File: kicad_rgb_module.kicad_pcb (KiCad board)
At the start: 2 copper layers, 25 x 25 mm, 37 parts, among them J1 Conn_HackConnect, SW1 TS-1088-AR02016, U1 STM32G030F6P6, U2 NCP114ASN330T1G

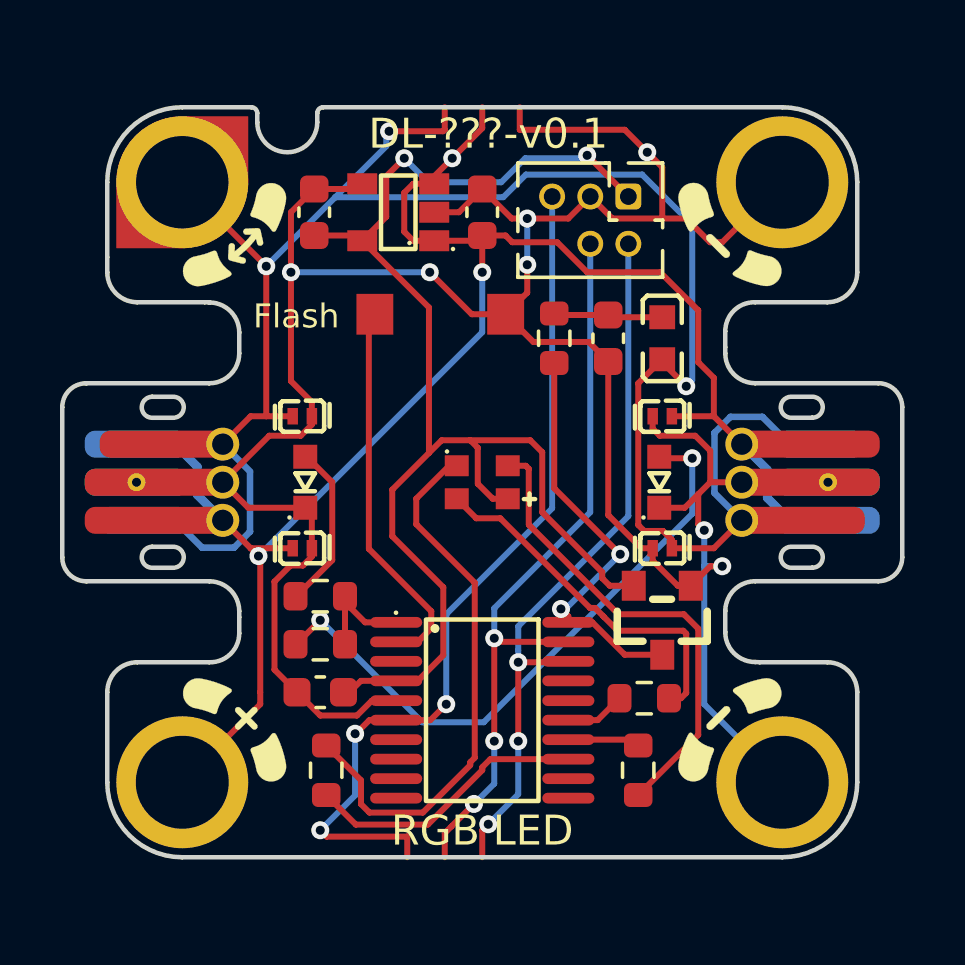
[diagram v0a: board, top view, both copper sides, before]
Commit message: Add diode to nRESET, decide on board sides for GerberSockets
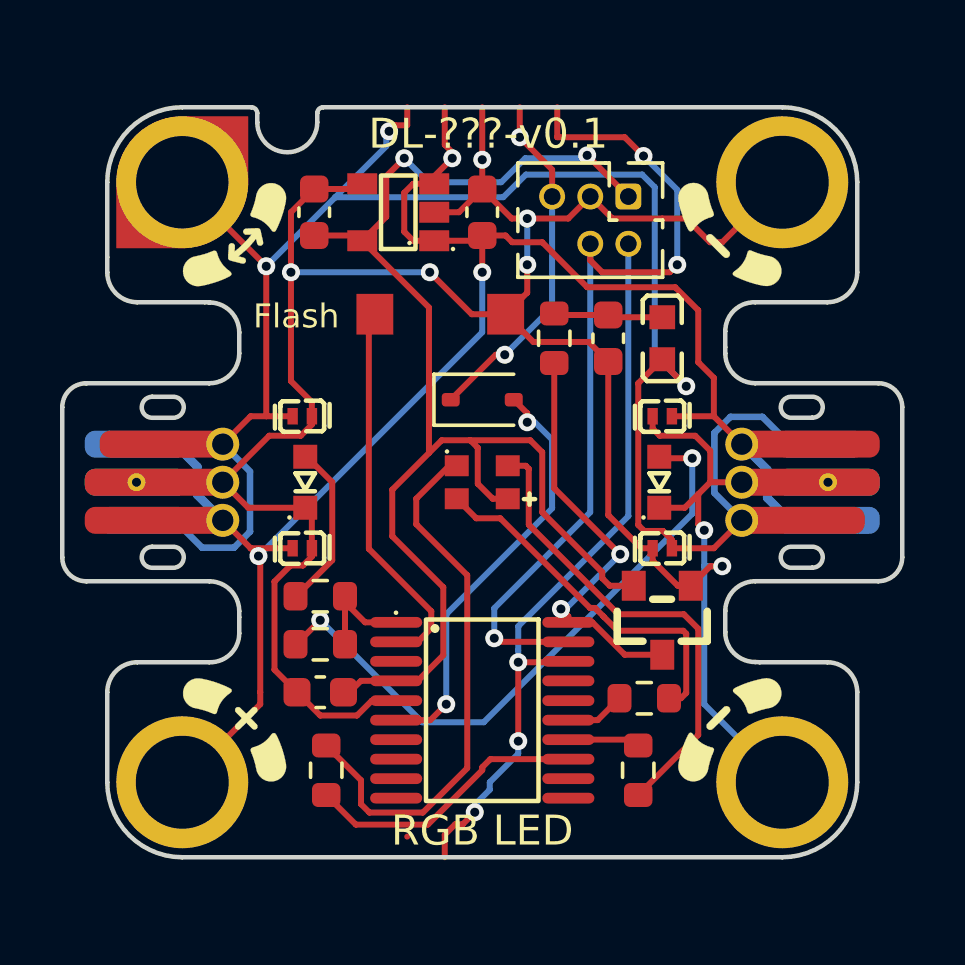
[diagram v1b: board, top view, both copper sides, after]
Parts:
- added D9: 1N4148WS, Diode_SMD:D_SOD-323, F.Cu at (85.5, 72.2)
- moved GS4 25.3 mm to (86.8, 62.5), turned to 180 degrees
- moved GS5 25.3 mm to (88.0, 62.5), turned to 180 degrees
- moved GS1 1.25 mm to (85.5, 62.5)
- moved GS2 1.25 mm to (83.0, 62.5)
- moved GS3 1.25 mm to (84.2, 62.5)
- moved GS6 1.25 mm to (84.2, 87.5)
- moved GS7 1.25 mm to (85.5, 87.5)
- moved GS8 1.25 mm to (86.8, 87.5)
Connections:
- GS4 pad 1: /nRESET -> /nRESET-SAFE
- J1 pad 5: /nRESET -> /nRESET-SAFE
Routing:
- net /nRESET: track 29.2 -> 14.2 mm, vias 3 -> 2
- net /nRESET-SAFE: track 0.00 -> 11.8 mm, vias 0 -> 2
- net GND: track 95.3 -> 90.3 mm
- net /SWCLK: track 25.2 -> 28.9 mm
- net /JD_DATA: track 50.3 -> 48.8 mm
- net /SWDIO: track 24.1 -> 24.8 mm

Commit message: Swap sides of GerberSockets, add devices-lab logo and hwidx QR code
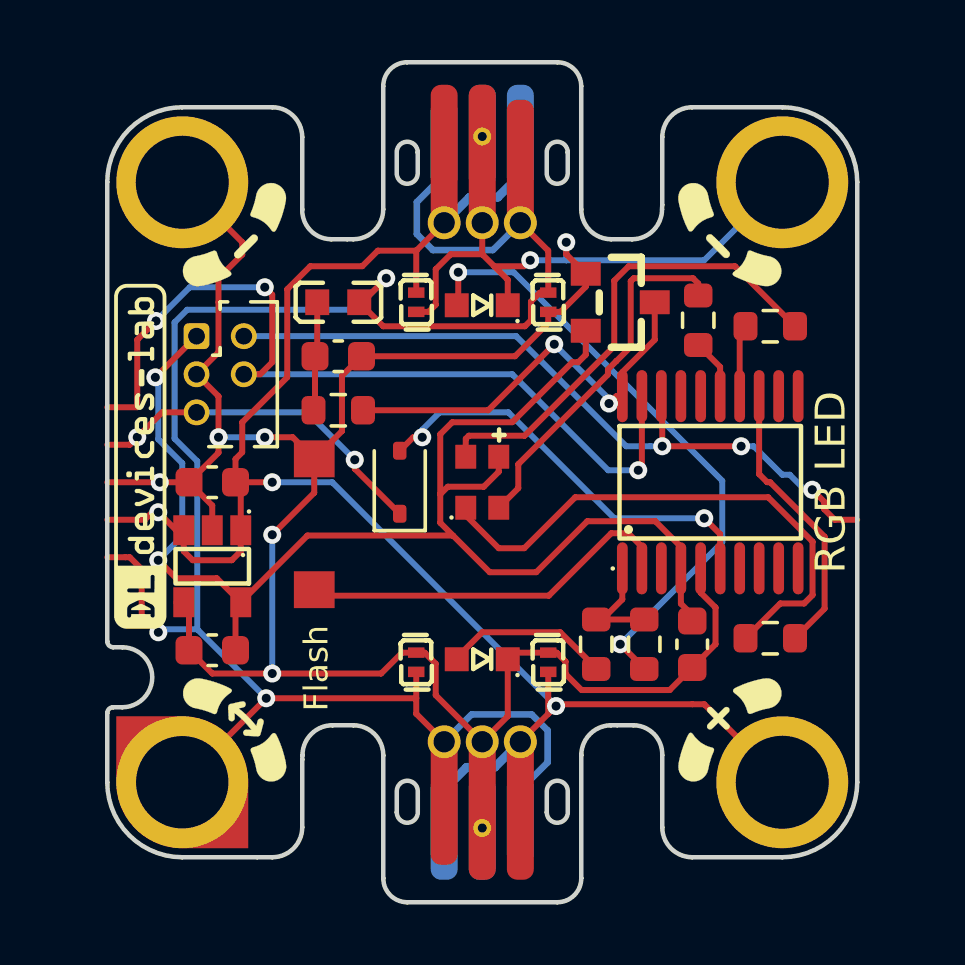
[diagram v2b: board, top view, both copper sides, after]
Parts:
- added G***: LOGO, LOGO, F.Cu at (74.1, 74.1)
- added G***: LOGO, LOGO, B.Cu at (85.5, 75.0)
- moved MH1 20.0 mm to (75.5, 85.0), turned to 90 degrees
- moved MH2 20.0 mm to (75.5, 65.0), turned to 90 degrees
- moved MH3 20.0 mm to (95.5, 85.0), turned to 90 degrees
- moved MH4 20.0 mm to (95.5, 65.0), turned to 90 degrees
- moved GS2 18.0 mm to (73.0, 77.5), turned to 90 degrees
- moved GS5 18.0 mm to (73.0, 72.5), turned to -90 degrees
- moved GS3 17.8 mm to (73.0, 76.2), turned to 90 degrees
- moved GS4 17.8 mm to (73.0, 73.8), turned to -90 degrees
- moved GS6 17.8 mm to (98.0, 76.2), turned to 90 degrees
- moved GS8 17.8 mm to (98.0, 73.8), turned to 90 degrees
- moved GS1 17.7 mm to (73.0, 75.0), turned to 90 degrees
- moved GS7 17.7 mm to (98.0, 75.0), turned to 90 degrees
- moved R4 15.4 mm to (95.1, 80.2), turned to 0 degrees
- moved R5 15.4 mm to (95.1, 69.8), turned to 180 degrees
- moved C4 15.0 mm to (76.5, 80.6), turned to 180 degrees
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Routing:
- net /JD_DATA: track 48.8 -> 49.5 mm
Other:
- outline, holes or cut-outs redrawn

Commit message: Set the correct LCSC components
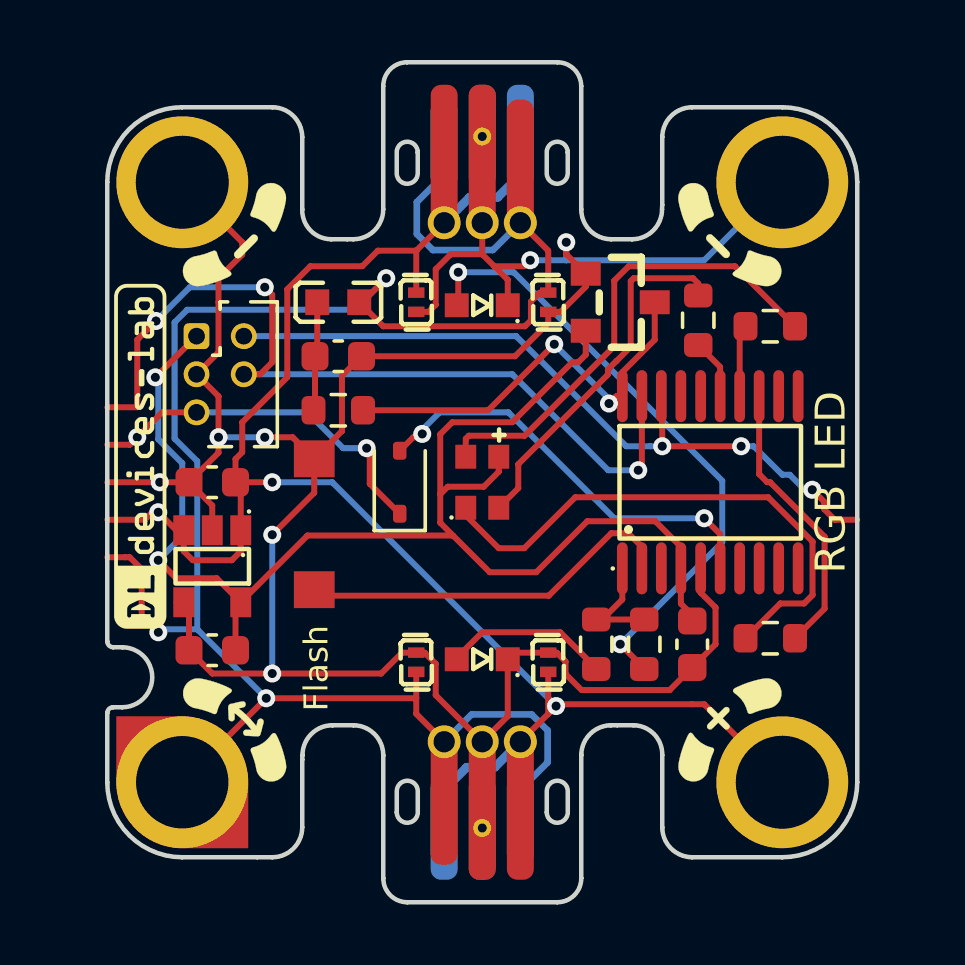
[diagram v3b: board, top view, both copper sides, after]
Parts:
- D8: value NH-B2020RGBA-HF -> NH-B2020RGBA-GF
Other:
- board text removed: "DL-???-v0.1"

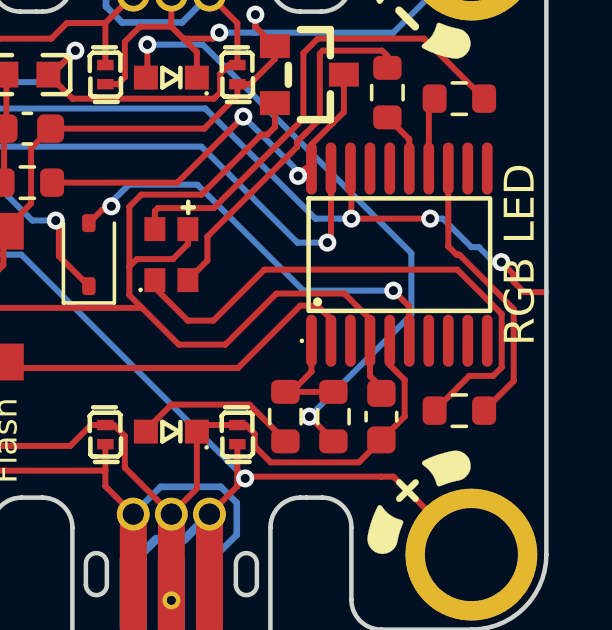
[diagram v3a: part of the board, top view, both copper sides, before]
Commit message: Change some GerberSockets and components
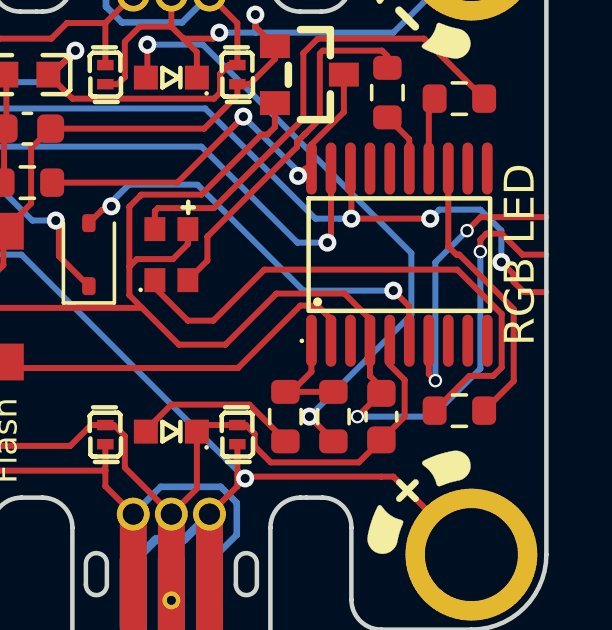
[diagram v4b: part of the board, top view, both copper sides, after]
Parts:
- GS7: value TEST_1 -> 3V3; footprint GerberSockets:TEST_1 -> GerberSockets:3V3
- GS8: value TEST_2 -> SERIAL; footprint GerberSockets:TEST_2 -> GerberSockets:SERIAL
- MH1: value jacdac_hole_DATA_MH1 -> Val**
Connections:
- GS7 pad 1: unconnected-(GS7-TEST_1-Pad1) -> +3V3
- GS8 pad 1: unconnected-(GS8-TEST_2-Pad1) -> /SERIAL
- U1 pad 7: unconnected-(U1-PA0-Pad7) -> /SERIAL
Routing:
- net +3V3: track 46.5 -> 59.3 mm, vias 2 -> 4
- net /SERIAL: track 0.00 -> 9.69 mm, vias 0 -> 2
- net /SWDIO: track 24.8 -> 25.7 mm

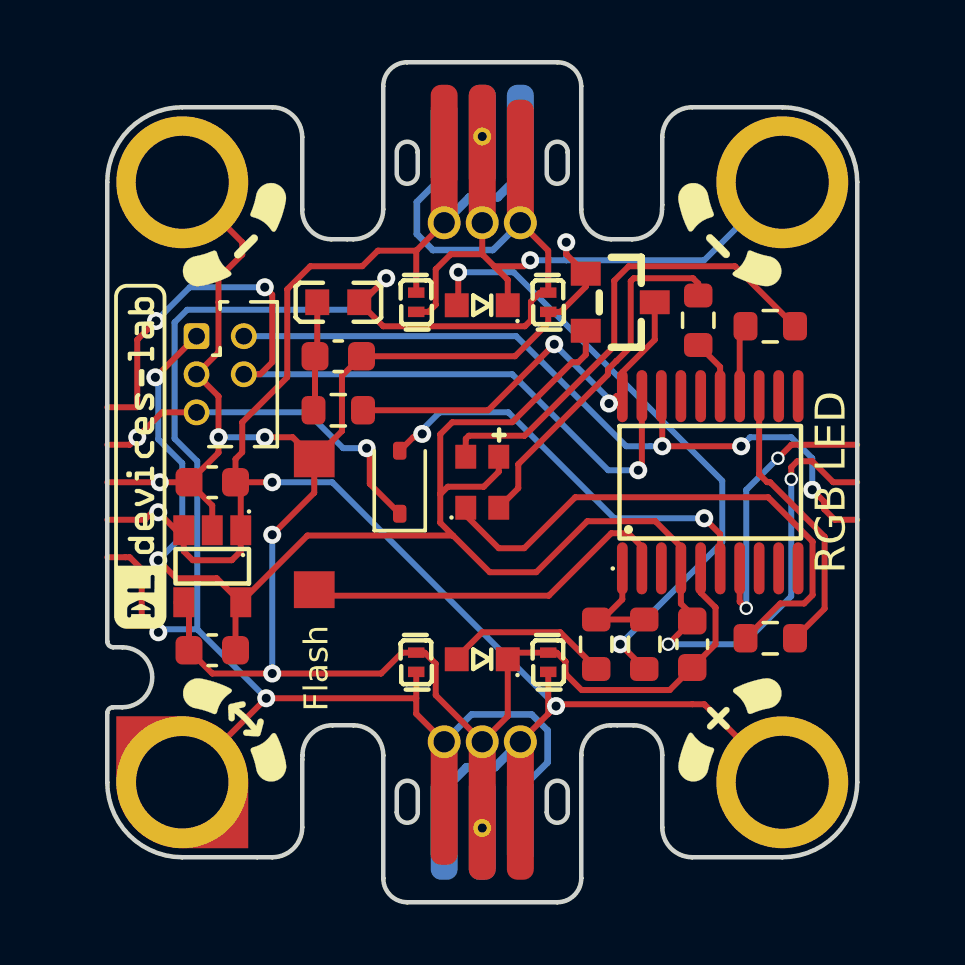
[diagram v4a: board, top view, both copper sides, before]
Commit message: Add test points
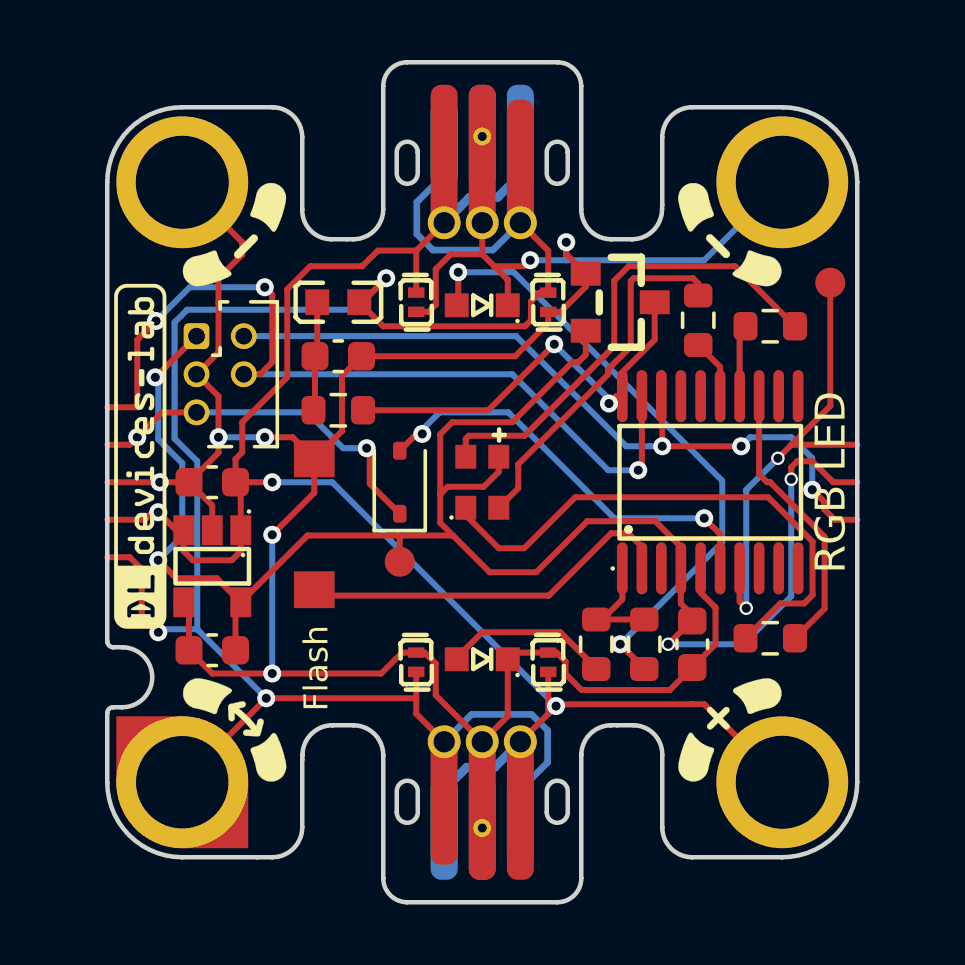
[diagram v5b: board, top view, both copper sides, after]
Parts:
- added TP1: TestPoint, Jacdac_Application:TestPoint_Pad_D1.0mm, F.Cu at (82.8, 77.7)
- added TP2: TestPoint, Jacdac_Application:TestPoint_Pad_D1.0mm, F.Cu at (97.1, 68.3)
- MH1: value Val** -> jacdac_hole_DATA_MH1
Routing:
- net /SERIAL: track 9.69 -> 15.6 mm
- net +3V3: track 59.3 -> 60.2 mm
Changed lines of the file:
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@@
 			)
 		)
-		(property "Value" "Val**"
+		(property "Value" "jacdac_hole_DATA_MH1"
 			(at 0.6 -3 90)
 			(layer "Cmts.User")
@@
 			)
 		)
-		(property "Description" ""
+		(property "Description" "Mounting Hole with connection"
 			(at 0 0 90)
 			(unlocked yes)
@@
 		(sheetname "/")
 		(sheetfile "kicad_rgb_module.kicad_sch")
-		(attr through_hole)
+		(attr through_hole exclude_from_bom)
 		(fp_circle
 			(center 0 0)
@@
 			(at 0.4 -4.8 0)
 			(layer "Cmts.User")
+			(hide yes)
 			(effects
 				(font
@@
 			)
 		)
-		(property "Description" "SERIAL GerberSocket"
+		(property "Description" "ASCII GerberSocket for net SERIAL"
 			(at 0 0 90)
 			(unlocked yes)
@@
 		(sheetname "/")
 		(sheetfile "kicad_rgb_module.kicad_sch")
-		(attr exclude_from_pos_files exclude_from_bom allow_missing_courtyard dnp)
+		(attr exclude_from_pos_files exclude_from_bom allow_missing_courtyard)
 		(fp_line
 			(start 0 -0.5)
@@
 			)
 		)
-		(property "Description" "3V3 GerberSocket"
+		(property "Description" "ASCII GerberSocket for net 3V3"
 			(at 0 0 90)
 			(unlocked yes)
@@
 		(sheetname "/")
 		(sheetfile "kicad_rgb_module.kicad_sch")
-		(attr exclude_from_pos_files exclude_from_bom allow_missing_courtyard dnp)
+		(attr exclude_from_pos_files exclude_from_bom allow_missing_courtyard)
 		(fp_line
 			(start 0 -0.5)
@@
 		(embedded_fonts no)
 	)
+	(footprint "Jacdac_Application:TestPoint_Pad_D1.0mm"
+		(layer "F.Cu")
+		(at 97.1 68.35)
+		(descr "SMD pad as test Point, diameter 1.0mm")
+		(tags "test point SMD pad")
+		(property "Reference" "TP2"
+			(at 0 -1.448 0)
+			(layer "F.SilkS")
+			(hide yes)
+			(effects
+				(font
+					(size 1 1)
+					(thickness 0.15)
+				)
+			)
+		)
+		(property "Value" "TestPoint"
+			(at 0 1.55 0)
+			(layer "F.Fab")
+			(hide yes)
+			(effects
+				(font
+					(size 1 1)
+					(thickness 0.15)
+				)
+			)
+		)
+		(property "Datasheet" ""
+			(at 0 0 0)
+			(unlocked yes)
+			(layer "F.Fab")
+			(hide yes)
+			(effects
+				(font
+					(size 1.27 1.27)
+					(thickness 0.15)
+				)
+			)
+		)
+		(property "Description" ""
+			(at 0 0 0)
+			(unlocked yes)
+			(layer "F.Fab")
+			(hide yes)
+			(effects
+				(font
+					(size 1.27 1.27)
+					(thickness 0.15)
+				)
+			)
+		)
+		(property ki_fp_filters "Pin* Test*")
+		(sheetname "/")
+		(sheetfile "kicad_rgb_module.kicad_sch")
+		(attr exclude_from_pos_files exclude_from_bom)
+		(pad "1" smd circle
+			(at 0 0)
+			(size 1 1)
+			(layers "F.Cu" "F.Mask")
+			(net 14 "/SERIAL")
+			(pinfunction "1")
+			(pintype "passive")
+		)
+		(embedded_fonts no)
+	)
+	(footprint "Jacdac_Application:TestPoint_Pad_D1.0mm"
+		(layer "F.Cu")
+		(at 82.75 77.65)
+		(descr "SMD pad as test Point, diameter 1.0mm")
+		(tags "test point SMD pad")
+		(property "Reference" "TP1"
+			(at 0 -1.448 0)
+			(layer "F.SilkS")
+			(hide yes)
+			(effects
+				(font
+					(size 1 1)
+					(thickness 0.15)
+				)
+			)
+		)
+		(property "Value" "TestPoint"
+			(at 0 1.55 0)
+			(layer "F.Fab")
+			(hide yes)
+			(effects
+				(font
+					(size 1 1)
+					(thickness 0.15)
+				)
+			)
+		)
+		(property "Datasheet" ""
+			(at 0 0 0)
+			(unlocked yes)
+			(layer "F.Fab")
+			(hide yes)
+			(effects
+				(font
+					(size 1.27 1.27)
+					(thickness 0.15)
+				)
+			)
+		)
+		(property "Description" ""
+			(at 0 0 0)
+			(unlocked yes)
+			(layer "F.Fab")
+			(hide yes)
+			(effects
+				(font
+					(size 1.27 1.27)
+					(thickness 0.15)
+				)
+			)
+		)
+		(property ki_fp_filters "Pin* Test*")
+		(sheetname "/")
+		(sheetfile "kicad_rgb_module.kicad_sch")
+		(attr exclude_from_pos_files exclude_from_bom)
+		(pad "1" smd circle
+			(at 0 0)
+			(size 1 1)
+			(layers "F.Cu" "F.Mask")
+			(net 2 "+3V3")
+			(pinfunction "1")
+			(pintype "passive")
+		)
+		(embedded_fonts no)
+	)
 	(footprint "Jacdac:jacdac_hole_GND_MH4"
 		(layer "F.Cu")
@@
 			(at 0.4 -4.8 0)
 			(layer "Cmts.User")
+			(hide yes)
 			(effects
 				(font
@@
 	)
 	(segment
+		(start 82.75 77.65)
+		(end 82.75 76.826)
+		(width 0.2)
+		(layer "F.Cu")
+		(net 2)
+	)
+	(segment
 		(start 92.12 79.045)
 		(end 92.7 79.625)
@@
 	(segment
 		(start 84.524 76.776)
+		(end 82.8 76.776)
+		(width 0.2)
+		(layer "F.Cu")
+		(net 2)
+	)
+	(segment
+		(start 82.7 76.776)
 		(end 79.674 76.776)
 		(width 0.2)
@@
 	)
 	(segment
+		(start 82.75 76.826)
+		(end 82.7 76.776)
+		(width 0.2)
+		(layer "F.Cu")
+		(net 2)
+	)
+	(segment
 		(start 91.268237 76.298)
 		(end 89.002 76.298)
@@
 	)
 	(segment
+		(start 82.8 76.776)
+		(end 82.7 76.776)
+		(width 0.2)
+		(layer "F.Cu")
+		(net 2)
+	)
+	(segment
 		(start 95.8 74.5)
 		(end 96 74.3)
@@
 	)
 	(segment
+		(start 97.1 72.456123)
+		(end 97.1 68.35)
+		(width 0.2)
+		(layer "F.Cu")
+		(net 14)
+	)
+	(segment
 		(start 95.806123 73.75)
 		(end 98 73.75)
 		(width 0.2)
 		(layer "F.Cu")
+		(net 14)
+	)
+	(segment
+		(start 95.806123 73.75)
+		(end 97.1 72.456123)
+		(width 0.2)
+		(layer "F.Cu")
